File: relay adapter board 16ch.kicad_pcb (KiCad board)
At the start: 2 copper layers, 13 parts, among them J1 RJ45_Shielded, J2 Screw_Terminal_01x02, J3 Conn_01x02_Pin, J4 Conn_02x10_Odd_Even, U3 TJA1051T-3

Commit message: Autosave
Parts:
- moved J4 43.2 mm to (150.5, 93.7)
- moved C1 2.00 mm to (104.5, 96.5)
- moved C2 2.00 mm to (105.5, 91.0)
- moved C3 2.00 mm to (103.5, 91.0)
- moved C4 2.00 mm to (101.5, 77.5)
- moved J1 2.00 mm to (102.2, 107.9)
- moved J2 2.00 mm to (105.5, 58.5)
- moved J3 2.00 mm to (106.5, 78.0)
- moved R2 2.00 mm to (101.5, 75.5)
- moved U3 2.00 mm to (104.0, 86.0)
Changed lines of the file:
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@@
 	(footprint "Connector_RJ:RJ45_Amphenol_54602-x08_Horizontal"
 		(layer "F.Cu")
-		(at 100.2175 107.9)
+		(at 102.2175 107.9)
 		(descr "8 Pol Shallow Latch Connector, Modjack, RJ45 (https://cdn.amphenol-icc.com/media/wysiwyg/files/drawing/c-bmj-0102.pdf)")
 		(tags "RJ45")
@@
 	(footprint "Capacitor_SMD:C_0402_1005Metric"
 		(layer "F.Cu")
-		(at 103.5 91 -90)
+		(at 105.5 91 -90)
 		(descr "Capacitor SMD 0402 (1005 Metric), square (rectangular) end terminal, IPC-7351 nominal, (Body size source: IPC-SM-782 page 76, https://www.pcb-3d.com/wordpress/wp-content/uploads/ipc-sm-782a_amendment_1_and_2.pdf)")
 		(tags "capacitor")
@@
 	(footprint "TerminalBlock_Phoenix:TerminalBlock_Phoenix_MKDS-1,5-2_1x02_P5.00mm_Horizontal"
 		(layer "F.Cu")
-		(at 103.5 58.5)
+		(at 105.5 58.5)
 		(descr "Terminal Block Phoenix MKDS-1,5-2, 2 pins, pitch 5mm, size 10x9.8mm, drill diameter 1.3mm, pad diameter 2.6mm, http://www.farnell.com/datasheets/100425.pdf")
 		(tags "THT Terminal Block Phoenix MKDS-1,5-2 pitch 5mm size 10x9.8mm drill 1.3mm pad 2.6mm")
@@
 	(footprint "Capacitor_SMD:C_0402_1005Metric"
 		(layer "F.Cu")
-		(at 99.5 77.52 -90)
+		(at 101.5 77.52 -90)
 		(descr "Capacitor SMD 0402 (1005 Metric), square (rectangular) end terminal, IPC-7351 nominal, (Body size source: IPC-SM-782 page 76, https://www.pcb-3d.com/wordpress/wp-content/uploads/ipc-sm-782a_amendment_1_and_2.pdf)")
 		(tags "capacitor")
@@
 	(footprint "Capacitor_SMD:C_Elec_6.3x5.8"
 		(layer "F.Cu")
-		(at 102.5 96.5 180)
+		(at 104.5 96.5 180)
 		(descr "SMD capacitor, aluminum electrolytic nonpolar, 6.3x5.8mm")
 		(tags "capacitor electrolytic nonpolar")
@@
 	(footprint "Capacitor_SMD:C_0402_1005Metric"
 		(layer "F.Cu")
-		(at 101.52 91 180)
+		(at 103.52 91 180)
 		(descr "Capacitor SMD 0402 (1005 Metric), square (rectangular) end terminal, IPC-7351 nominal, (Body size source: IPC-SM-782 page 76, https://www.pcb-3d.com/wordpress/wp-content/uploads/ipc-sm-782a_amendment_1_and_2.pdf)")
 		(tags "capacitor")
@@
 	(footprint "Connector_PinHeader_2.54mm:PinHeader_1x02_P2.54mm_Vertical"
 		(layer "F.Cu")
-		(at 104.525 78.02 180)
+		(at 106.525 78.02 180)
 		(descr "Through hole straight pin header, 1x02, 2.54mm pitch, single row")
 		(tags "Through hole pin header THT 1x02 2.54mm single row")
@@
 	(footprint "Capacitor_SMD:C_0402_1005Metric"
 		(layer "F.Cu")
-		(at 99.5 75.52 90)
+		(at 101.5 75.52 90)
 		(descr "Capacitor SMD 0402 (1005 Metric), square (rectangular) end terminal, IPC-7351 nominal, (Body size source: IPC-SM-782 page 76, https://www.pcb-3d.com/wordpress/wp-content/uploads/ipc-sm-782a_amendment_1_and_2.pdf)")
 		(tags "capacitor")
@@
 	(footprint "Package_SO:SOIC-8_3.9x4.9mm_P1.27mm"
 		(layer "F.Cu")
-		(at 102 86 90)
+		(at 104 86 90)
 		(descr "SOIC, 8 Pin (JEDEC MS-012AA, https://www.analog.com/media/en/package-pcb-resources/package/pkg_pdf/soic_narrow-r/r_8.pdf)")
 		(tags "SOIC SO")
@@
 	(footprint "Connector_PinSocket_2.54mm:PinSocket_2x10_P2.54mm_Vertical"
 		(layer "B.Cu")
-		(at 193.54 89.58)
+		(at 150.54 93.66)
 		(descr "Through hole straight socket strip, 2x10, 2.54mm pitch, double rows (from Kicad 4.0.7), script generated")
 		(tags "Through hole socket strip THT 2x10 2.54mm double row")

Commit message: Autosave
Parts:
- moved J4 22.8 mm to (148.5, 70.9), turned to 180 degrees
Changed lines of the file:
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@@
 	(footprint "Connector_PinSocket_2.54mm:PinSocket_2x10_P2.54mm_Vertical"
 		(layer "B.Cu")
-		(at 150.54 93.66)
+		(at 148.5 70.92 180)
 		(descr "Through hole straight socket strip, 2x10, 2.54mm pitch, double rows (from Kicad 4.0.7), script generated")
 		(tags "Through hole socket strip THT 2x10 2.54mm double row")
@@
 		(duplicate_pad_numbers_are_jumpers no)
 		(fp_line
+			(start 1.33 1.33)
+			(end 1.33 0)
+			(stroke
+				(width 0.12)
+				(type solid)
+			)
+			(layer "B.SilkS")
+		)
+		(fp_line
+			(start 1.33 -1.27)
+			(end 1.33 -24.19)
+			(stroke
+				(width 0.12)
+				(type solid)
+			)
+			(layer "B.SilkS")
+		)
+		(fp_line
+			(start 0 1.33)
+			(end 1.33 1.33)
+			(stroke
+				(width 0.12)
+				(type solid)
+			)
+			(layer "B.SilkS")
+		)
+		(fp_line
+			(start -1.27 1.33)
+			(end -1.27 -1.27)
+			(stroke
+				(width 0.12)
+				(type solid)
+			)
+			(layer "B.SilkS")
+		)
+		(fp_line
+			(start -1.27 -1.27)
+			(end 1.33 -1.27)
+			(stroke
+				(width 0.12)
+				(type solid)
+			)
+			(layer "B.SilkS")
+		)
+		(fp_line
+			(start -3.87 1.33)
+			(end -1.27 1.33)
+			(stroke
+				(width 0.12)
+				(type solid)
+			)
+			(layer "B.SilkS")
+		)
+		(fp_line
+			(start -3.87 1.33)
+			(end -3.87 -24.19)
+			(stroke
+				(width 0.12)
+				(type solid)
+			)
+			(layer "B.SilkS")
+		)
+		(fp_line
 			(start -3.87 -24.19)
 			(end 1.33 -24.19)
@@
 		)
 		(fp_line
-			(start -3.87 1.33)
-			(end -3.87 -24.19)
-			(stroke
-				(width 0.12)
-				(type solid)
-			)
-			(layer "B.SilkS")
-		)
-		(fp_line
-			(start -3.87 1.33)
-			(end -1.27 1.33)
-			(stroke
-				(width 0.12)
-				(type solid)
-			)
-			(layer "B.SilkS")
-		)
-		(fp_line
-			(start -1.27 -1.27)
-			(end 1.33 -1.27)
-			(stroke
-				(width 0.12)
-				(type solid)
-			)
-			(layer "B.SilkS")
-		)
-		(fp_line
-			(start -1.27 1.33)
-			(end -1.27 -1.27)
-			(stroke
-				(width 0.12)
-				(type solid)
-			)
-			(layer "B.SilkS")
-		)
-		(fp_line
-			(start 0 1.33)
-			(end 1.33 1.33)
-			(stroke
-				(width 0.12)
-				(type solid)
-			)
-			(layer "B.SilkS")
-		)
-		(fp_line
-			(start 1.33 -1.27)
-			(end 1.33 -24.19)
-			(stroke
-				(width 0.12)
-				(type solid)
-			)
-			(layer "B.SilkS")
-		)
-		(fp_line
-			(start 1.33 1.33)
-			(end 1.33 0)
-			(stroke
-				(width 0.12)
-				(type solid)
-			)
-			(layer "B.SilkS")
+			(start 1.77 1.77)
+			(end 1.77 -24.63)
+			(stroke
+				(width 0.05)
+				(type solid)
+			)
+			(layer "B.CrtYd")
+		)
+		(fp_line
+			(start 1.77 -24.63)
+			(end -4.31 -24.63)
+			(stroke
+				(width 0.05)
+				(type solid)
+			)
+			(layer "B.CrtYd")
+		)
+		(fp_line
+			(start -4.31 1.77)
+			(end 1.77 1.77)
+			(stroke
+				(width 0.05)
+				(type solid)
+			)
+			(layer "B.CrtYd")
 		)
 		(fp_line
@@
 		)
 		(fp_line
-			(start -4.31 1.77)
-			(end 1.77 1.77)
-			(stroke
-				(width 0.05)
-				(type solid)
-			)
-			(layer "B.CrtYd")
-		)
-		(fp_line
-			(start 1.77 -24.63)
-			(end -4.31 -24.63)
-			(stroke
-				(width 0.05)
-				(type solid)
-			)
-			(layer "B.CrtYd")
-		)
-		(fp_line
-			(start 1.77 1.77)
-			(end 1.77 -24.63)
-			(stroke
-				(width 0.05)
-				(type solid)
-			)
-			(layer "B.CrtYd")
+			(start 1.27 0.27)
+			(end 1.27 -24.13)
+			(stroke
+				(width 0.1)
+				(type solid)
+			)
+			(layer "B.Fab")
+		)
+		(fp_line
+			(start 1.27 -24.13)
+			(end -3.81 -24.13)
+			(stroke
+				(width 0.1)
+				(type solid)
+			)
+			(layer "B.Fab")
+		)
+		(fp_line
+			(start 0.27 1.27)
+			(end 1.27 0.27)
+			(stroke
+				(width 0.1)
+				(type solid)
+			)
+			(layer "B.Fab")
+		)
+		(fp_line
+			(start -3.81 1.27)
+			(end 0.27 1.27)
+			(stroke
+				(width 0.1)
+				(type solid)
+			)
+			(layer "B.Fab")
 		)
 		(fp_line
@@
 			(layer "B.Fab")
 		)
-		(fp_line
-			(start -3.81 1.27)
-			(end 0.27 1.27)
-			(stroke
-				(width 0.1)
-				(type solid)
-			)
-			(layer "B.Fab")
-		)
-		(fp_line
-			(start 0.27 1.27)
-			(end 1.27 0.27)
-			(stroke
-				(width 0.1)
-				(type solid)
-			)
-			(layer "B.Fab")
-		)
-		(fp_line
-			(start 1.27 -24.13)
-			(end -3.81 -24.13)
-			(stroke
-				(width 0.1)
-				(type solid)
-			)
-			(layer "B.Fab")
-		)
-		(fp_line
-			(start 1.27 0.27)
-			(end 1.27 -24.13)
-			(stroke
-				(width 0.1)
-				(type solid)
-			)
-			(layer "B.Fab")
-		)
 		(fp_text user "${REFERENCE}"
 			(at -1.27 -11.43 90)
@@
 		)
 		(pad "1" thru_hole rect
-			(at 0 0)
+			(at 0 0 180)
 			(size 1.7 1.7)
 			(drill 1)
@@
 		)
 		(pad "2" thru_hole circle
-			(at -2.54 0)
+			(at -2.54 0 180)
 			(size 1.7 1.7)
 			(drill 1)
@@
 		)
 		(pad "3" thru_hole circle
-			(at 0 -2.54)
+			(at 0 -2.54 180)
 			(size 1.7 1.7)
 			(drill 1)
@@
 		)
 		(pad "4" thru_hole circle
-			(at -2.54 -2.54)
+			(at -2.54 -2.54 180)
 			(size 1.7 1.7)
 			(drill 1)
@@
 		)
 		(pad "5" thru_hole circle
-			(at 0 -5.08)
+			(at 0 -5.08 180)
 			(size 1.7 1.7)
 			(drill 1)
@@
 		)
 		(pad "6" thru_hole circle
-			(at -2.54 -5.08)
+			(at -2.54 -5.08 180)
 			(size 1.7 1.7)
 			(drill 1)
@@
 		)
 		(pad "7" thru_hole circle
-			(at 0 -7.62)
+			(at 0 -7.62 180)
 			(size 1.7 1.7)
 			(drill 1)
@@
 		)
 		(pad "8" thru_hole circle
-			(at -2.54 -7.62)
+			(at -2.54 -7.62 180)
 			(size 1.7 1.7)
 			(drill 1)
@@
 		)
 		(pad "9" thru_hole circle
-			(at 0 -10.16)
+			(at 0 -10.16 180)
 			(size 1.7 1.7)
 			(drill 1)
@@
 		)
 		(pad "10" thru_hole circle
-			(at -2.54 -10.16)
+			(at -2.54 -10.16 180)
 			(size 1.7 1.7)
 			(drill 1)
@@
 		)
 		(pad "11" thru_hole circle
-			(at 0 -12.7)
+			(at 0 -12.7 180)
 			(size 1.7 1.7)
 			(drill 1)
@@
 		)
 		(pad "12" thru_hole circle
-			(at -2.54 -12.7)
+			(at -2.54 -12.7 180)
 			(size 1.7 1.7)
 			(drill 1)
@@
 		)
 		(pad "13" thru_hole circle
-			(at 0 -15.24)
+			(at 0 -15.24 180)
 			(size 1.7 1.7)
 			(drill 1)
@@
 		)
 		(pad "14" thru_hole circle
-			(at -2.54 -15.24)
+			(at -2.54 -15.24 180)
 			(size 1.7 1.7)
 			(drill 1)
@@
 		)
 		(pad "15" thru_hole circle
-			(at 0 -17.78)
+			(at 0 -17.78 180)
 			(size 1.7 1.7)
 			(drill 1)
@@
 		)
 		(pad "16" thru_hole circle
-			(at -2.54 -17.78)
+			(at -2.54 -17.78 180)
 			(size 1.7 1.7)
 			(drill 1)
@@
 		)
 		(pad "17" thru_hole circle
-			(at 0 -20.32)
+			(at 0 -20.32 180)
 			(size 1.7 1.7)
 			(drill 1)
@@
 		)
 		(pad "18" thru_hole circle
-			(at -2.54 -20.32)
+			(at -2.54 -20.32 180)
 			(size 1.7 1.7)
 			(drill 1)
@@
 		)
 		(pad "19" thru_hole circle
-			(at 0 -22.86)
+			(at 0 -22.86 180)
 			(size 1.7 1.7)
 			(drill 1)
@@
 		)
 		(pad "20" thru_hole circle
-			(at -2.54 -22.86)
-			(size 1.7 1.7)
-			(drill 1)
+			(at -2.54 -22.86 180)
+			(size 1.7 1.7)
+			(drill 1)

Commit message: Autosave
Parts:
- turned STM32F103C6T1 to -90 degrees

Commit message: Autosave
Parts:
- moved C3 63.1 mm to (166.5, 93.7)
- moved C1 63.1 mm to (167.5, 99.2)
- moved C2 63.1 mm to (168.5, 93.7)
- moved C4 63.1 mm to (164.5, 80.2)
- moved J1 63.1 mm to (165.2, 110.6)
- moved J2 63.1 mm to (168.5, 61.2)
- moved J3 63.1 mm to (169.5, 80.7)
- moved R2 63.1 mm to (164.5, 78.2)
- moved U3 63.1 mm to (167.0, 88.7)
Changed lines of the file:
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@@
 	(footprint "Connector_RJ:RJ45_Amphenol_54602-x08_Horizontal"
 		(layer "F.Cu")
-		(at 102.2175 107.9)
+		(at 165.2175 110.5725)
 		(descr "8 Pol Shallow Latch Connector, Modjack, RJ45 (https://cdn.amphenol-icc.com/media/wysiwyg/files/drawing/c-bmj-0102.pdf)")
 		(tags "RJ45")
@@
 	(footprint "Capacitor_SMD:C_0402_1005Metric"
 		(layer "F.Cu")
-		(at 105.5 91 -90)
+		(at 168.5 93.6725 -90)
 		(descr "Capacitor SMD 0402 (1005 Metric), square (rectangular) end terminal, IPC-7351 nominal, (Body size source: IPC-SM-782 page 76, https://www.pcb-3d.com/wordpress/wp-content/uploads/ipc-sm-782a_amendment_1_and_2.pdf)")
 		(tags "capacitor")
@@
 	(footprint "TerminalBlock_Phoenix:TerminalBlock_Phoenix_MKDS-1,5-2_1x02_P5.00mm_Horizontal"
 		(layer "F.Cu")
-		(at 105.5 58.5)
+		(at 168.5 61.1725)
 		(descr "Terminal Block Phoenix MKDS-1,5-2, 2 pins, pitch 5mm, size 10x9.8mm, drill diameter 1.3mm, pad diameter 2.6mm, http://www.farnell.com/datasheets/100425.pdf")
 		(tags "THT Terminal Block Phoenix MKDS-1,5-2 pitch 5mm size 10x9.8mm drill 1.3mm pad 2.6mm")
@@
 	(footprint "Capacitor_SMD:C_0402_1005Metric"
 		(layer "F.Cu")
-		(at 101.5 77.52 -90)
+		(at 164.5 80.1925 -90)
 		(descr "Capacitor SMD 0402 (1005 Metric), square (rectangular) end terminal, IPC-7351 nominal, (Body size source: IPC-SM-782 page 76, https://www.pcb-3d.com/wordpress/wp-content/uploads/ipc-sm-782a_amendment_1_and_2.pdf)")
 		(tags "capacitor")
@@
 	(footprint "Capacitor_SMD:C_Elec_6.3x5.8"
 		(layer "F.Cu")
-		(at 104.5 96.5 180)
+		(at 167.5 99.1725 180)
 		(descr "SMD capacitor, aluminum electrolytic nonpolar, 6.3x5.8mm")
 		(tags "capacitor electrolytic nonpolar")
@@
 	(footprint "Capacitor_SMD:C_0402_1005Metric"
 		(layer "F.Cu")
-		(at 103.52 91 180)
+		(at 166.52 93.6725 180)
 		(descr "Capacitor SMD 0402 (1005 Metric), square (rectangular) end terminal, IPC-7351 nominal, (Body size source: IPC-SM-782 page 76, https://www.pcb-3d.com/wordpress/wp-content/uploads/ipc-sm-782a_amendment_1_and_2.pdf)")
 		(tags "capacitor")
@@
 	(footprint "Connector_PinHeader_2.54mm:PinHeader_1x02_P2.54mm_Vertical"
 		(layer "F.Cu")
-		(at 106.525 78.02 180)
+		(at 169.525 80.6925 180)
 		(descr "Through hole straight pin header, 1x02, 2.54mm pitch, single row")
 		(tags "Through hole pin header THT 1x02 2.54mm single row")
@@
 	(footprint "Capacitor_SMD:C_0402_1005Metric"
 		(layer "F.Cu")
-		(at 101.5 75.52 90)
+		(at 164.5 78.1925 90)
 		(descr "Capacitor SMD 0402 (1005 Metric), square (rectangular) end terminal, IPC-7351 nominal, (Body size source: IPC-SM-782 page 76, https://www.pcb-3d.com/wordpress/wp-content/uploads/ipc-sm-782a_amendment_1_and_2.pdf)")
 		(tags "capacitor")
@@
 	(footprint "Package_SO:SOIC-8_3.9x4.9mm_P1.27mm"
 		(layer "F.Cu")
-		(at 104 86 90)
+		(at 167 88.6725 90)
 		(descr "SOIC, 8 Pin (JEDEC MS-012AA, https://www.analog.com/media/en/package-pcb-resources/package/pkg_pdf/soic_narrow-r/r_8.pdf)")
 		(tags "SOIC SO")

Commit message: Autosave
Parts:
- moved C3 61.5 mm to (105.1, 90.2)
- moved J3 61.5 mm to (108.1, 77.3)
- moved C1 61.5 mm to (106.1, 95.8)
- moved C2 61.5 mm to (107.1, 90.2)
- moved C4 61.5 mm to (103.1, 76.8)
- moved J1 61.5 mm to (103.8, 107.2)
- moved J2 61.5 mm to (107.1, 57.8)
- moved R2 61.5 mm to (103.1, 74.8)
- moved U3 61.5 mm to (105.6, 85.2)
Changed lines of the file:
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@@
 	(footprint "Connector_RJ:RJ45_Amphenol_54602-x08_Horizontal"
 		(layer "F.Cu")
-		(at 165.2175 110.5725)
+		(at 103.84 107.15)
 		(descr "8 Pol Shallow Latch Connector, Modjack, RJ45 (https://cdn.amphenol-icc.com/media/wysiwyg/files/drawing/c-bmj-0102.pdf)")
 		(tags "RJ45")
@@
 	(footprint "Capacitor_SMD:C_0402_1005Metric"
 		(layer "F.Cu")
-		(at 168.5 93.6725 -90)
+		(at 107.1225 90.25 -90)
 		(descr "Capacitor SMD 0402 (1005 Metric), square (rectangular) end terminal, IPC-7351 nominal, (Body size source: IPC-SM-782 page 76, https://www.pcb-3d.com/wordpress/wp-content/uploads/ipc-sm-782a_amendment_1_and_2.pdf)")
 		(tags "capacitor")
@@
 	(footprint "TerminalBlock_Phoenix:TerminalBlock_Phoenix_MKDS-1,5-2_1x02_P5.00mm_Horizontal"
 		(layer "F.Cu")
-		(at 168.5 61.1725)
+		(at 107.1225 57.75)
 		(descr "Terminal Block Phoenix MKDS-1,5-2, 2 pins, pitch 5mm, size 10x9.8mm, drill diameter 1.3mm, pad diameter 2.6mm, http://www.farnell.com/datasheets/100425.pdf")
 		(tags "THT Terminal Block Phoenix MKDS-1,5-2 pitch 5mm size 10x9.8mm drill 1.3mm pad 2.6mm")
@@
 	(footprint "Capacitor_SMD:C_0402_1005Metric"
 		(layer "F.Cu")
-		(at 164.5 80.1925 -90)
+		(at 103.1225 76.77 -90)
 		(descr "Capacitor SMD 0402 (1005 Metric), square (rectangular) end terminal, IPC-7351 nominal, (Body size source: IPC-SM-782 page 76, https://www.pcb-3d.com/wordpress/wp-content/uploads/ipc-sm-782a_amendment_1_and_2.pdf)")
 		(tags "capacitor")
@@
 	(footprint "Capacitor_SMD:C_Elec_6.3x5.8"
 		(layer "F.Cu")
-		(at 167.5 99.1725 180)
+		(at 106.1225 95.75 180)
 		(descr "SMD capacitor, aluminum electrolytic nonpolar, 6.3x5.8mm")
 		(tags "capacitor electrolytic nonpolar")
@@
 	(footprint "Capacitor_SMD:C_0402_1005Metric"
 		(layer "F.Cu")
-		(at 166.52 93.6725 180)
+		(at 105.1425 90.25 180)
 		(descr "Capacitor SMD 0402 (1005 Metric), square (rectangular) end terminal, IPC-7351 nominal, (Body size source: IPC-SM-782 page 76, https://www.pcb-3d.com/wordpress/wp-content/uploads/ipc-sm-782a_amendment_1_and_2.pdf)")
 		(tags "capacitor")
@@
 	(footprint "Connector_PinHeader_2.54mm:PinHeader_1x02_P2.54mm_Vertical"
 		(layer "F.Cu")
-		(at 169.525 80.6925 180)
+		(at 108.1475 77.27 180)
 		(descr "Through hole straight pin header, 1x02, 2.54mm pitch, single row")
 		(tags "Through hole pin header THT 1x02 2.54mm single row")
@@
 	(footprint "Capacitor_SMD:C_0402_1005Metric"
 		(layer "F.Cu")
-		(at 164.5 78.1925 90)
+		(at 103.1225 74.77 90)
 		(descr "Capacitor SMD 0402 (1005 Metric), square (rectangular) end terminal, IPC-7351 nominal, (Body size source: IPC-SM-782 page 76, https://www.pcb-3d.com/wordpress/wp-content/uploads/ipc-sm-782a_amendment_1_and_2.pdf)")
 		(tags "capacitor")
@@
 	(footprint "Package_SO:SOIC-8_3.9x4.9mm_P1.27mm"
 		(layer "F.Cu")
-		(at 167 88.6725 90)
+		(at 105.6225 85.25 90)
 		(descr "SOIC, 8 Pin (JEDEC MS-012AA, https://www.analog.com/media/en/package-pcb-resources/package/pkg_pdf/soic_narrow-r/r_8.pdf)")
 		(tags "SOIC SO")

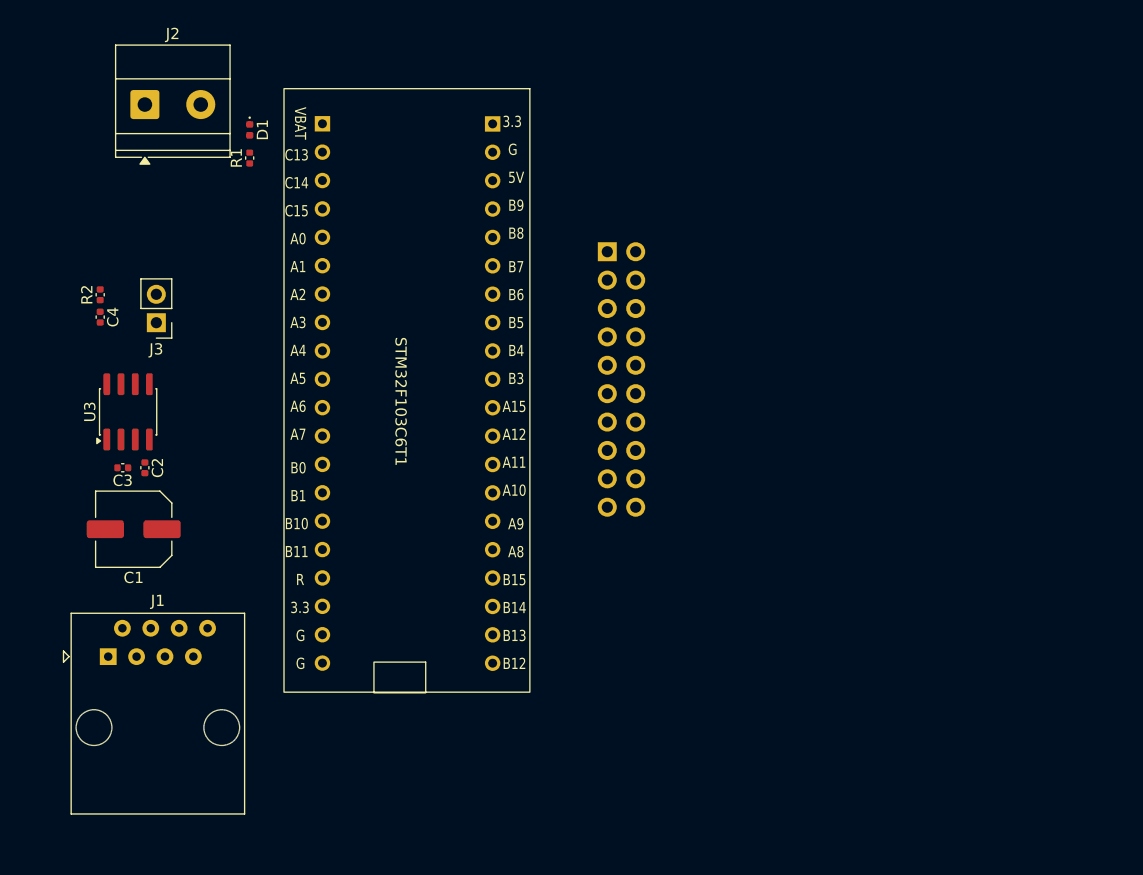
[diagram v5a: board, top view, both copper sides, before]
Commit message: SCH Save: 2 files changed relay adapter board 16ch.kicad_pcb 0/6/4360 relay adapter board 16ch.kicad_sch 0/0/7876
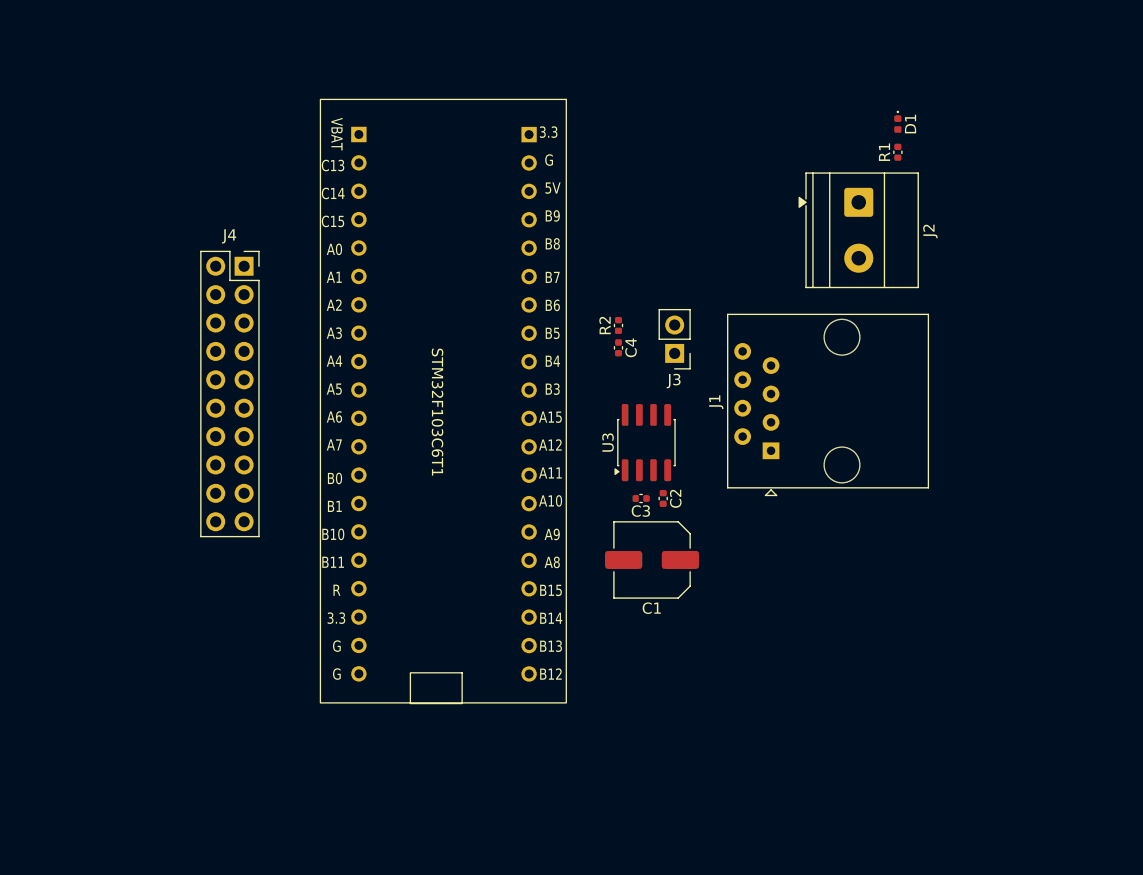
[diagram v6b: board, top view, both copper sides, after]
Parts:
- J4: moved to F.Cu
- moved J2 64.5 mm to (171.0, 66.5), turned to -90 degrees
- moved J1 62.1 mm to (163.2, 88.7), turned to 90 degrees
- moved D1 58.0 mm to (174.5, 59.5)
- moved R1 58.0 mm to (174.5, 62.0)
- moved C3 46.5 mm to (151.5, 93.0)
- moved J3 46.5 mm to (154.5, 80.0)
- moved C1 46.5 mm to (152.5, 98.5)
- moved C2 46.5 mm to (153.5, 93.0)
- moved C4 46.5 mm to (149.5, 79.5)
- moved R2 46.5 mm to (149.5, 77.5)
- moved U3 46.5 mm to (152.0, 88.0)
- moved J4 32.5 mm to (116.0, 72.2), turned to 0 degrees
- moved STM32F103C6T1 3.40 mm to (133.9, 84.3)

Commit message: Autosave
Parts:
- J4: moved to B.Cu
- moved J4 7.04 mm to (109.0, 72.3), turned to 180 degrees
